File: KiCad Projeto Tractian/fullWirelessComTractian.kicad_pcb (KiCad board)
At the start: 4 copper layers, 46.8 x 53.3 mm, 28 parts, among them U1 ESP8266EX, U2 MX25R3235FM2xx1, U4 MX25R3235FM2xx1, U5 AMS1117-3.3, U6 TMP36xS, Y2 XTAL 16Mhz ±10ppm (TSX -3225 )

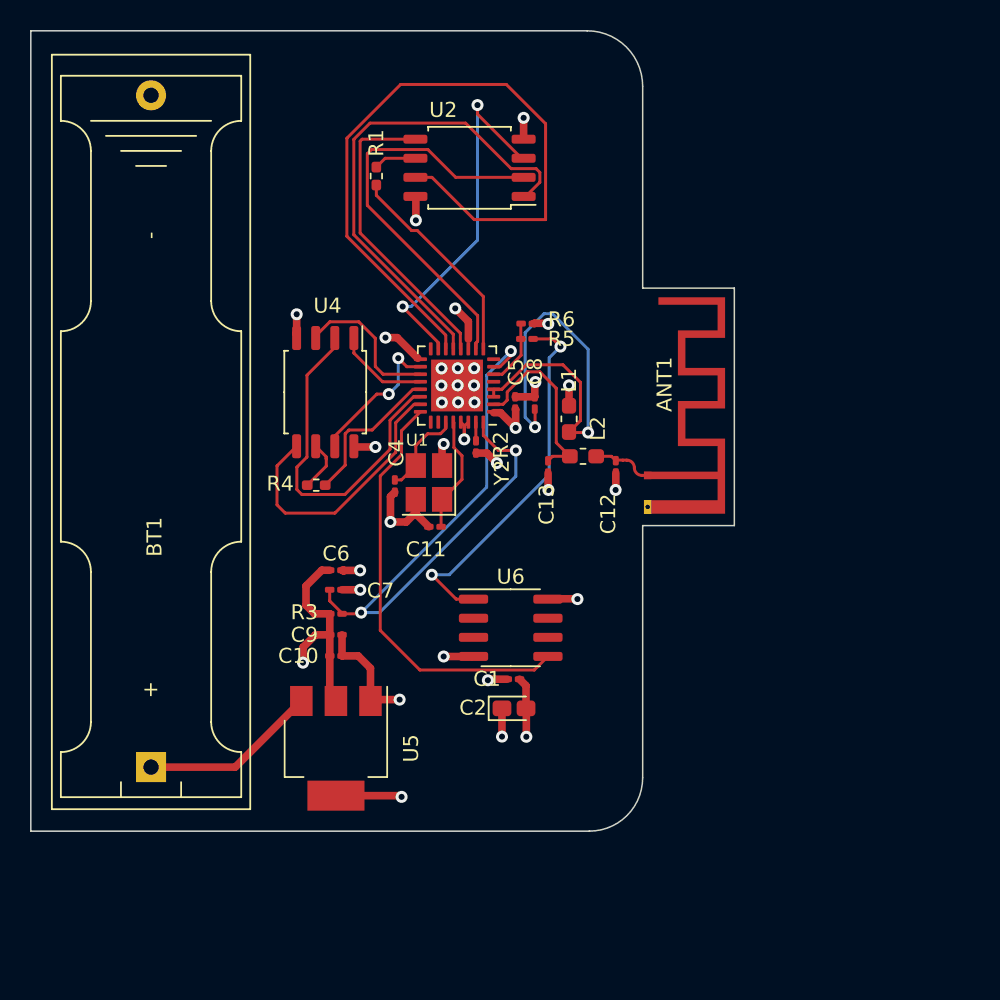
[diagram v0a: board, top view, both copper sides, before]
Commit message: :construction: Add tantos GND vias quanto possível para melhor aterramento -  RF design ESP datasheet
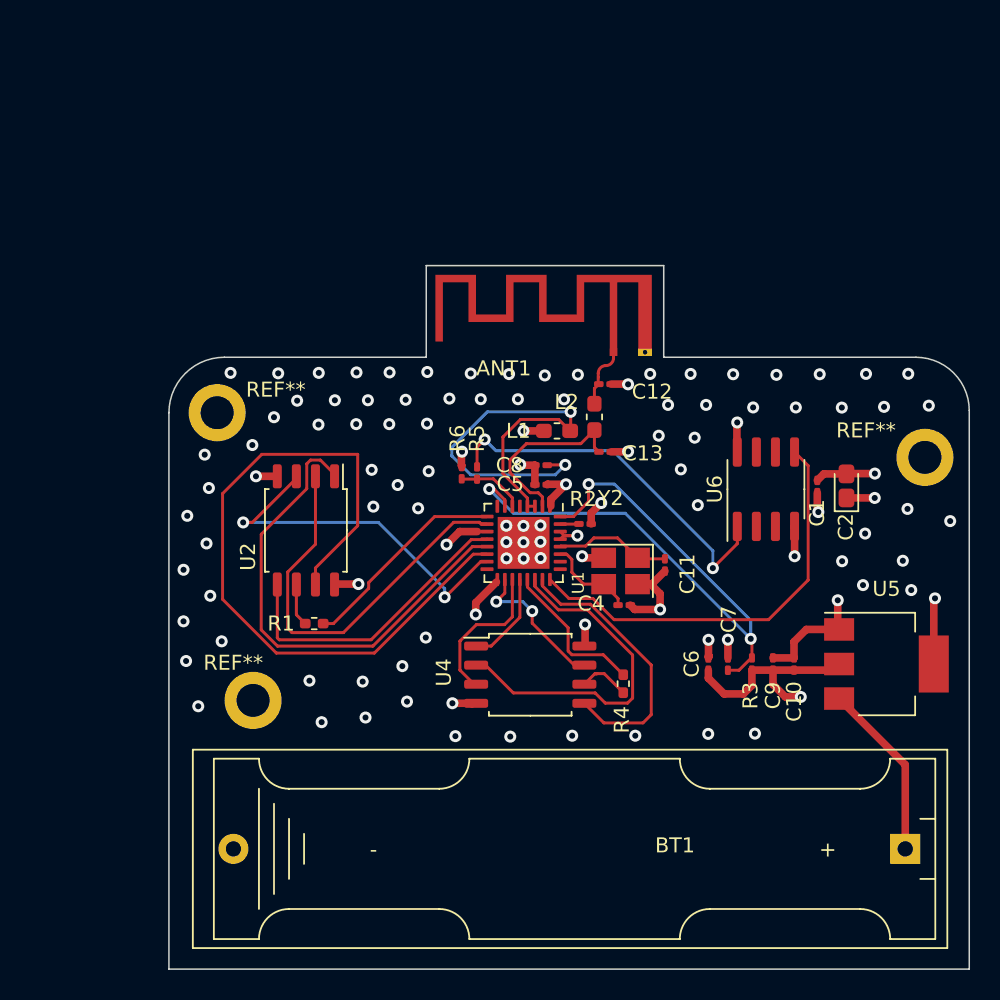
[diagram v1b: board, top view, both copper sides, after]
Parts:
- added REF**: MountingHole_2.2mm_M2_DIN965_Pad, MountingHole:MountingHole_2.2mm_M2_DIN965_Pad, F.Cu at (178.5, 99.2)
- added REF**: MountingHole_2.2mm_M2_DIN965_Pad, MountingHole:MountingHole_2.2mm_M2_DIN965_Pad, F.Cu at (131.4, 96.2)
- added REF**: MountingHole_2.2mm_M2_DIN965_Pad, MountingHole:MountingHole_2.2mm_M2_DIN965_Pad, F.Cu at (133.8, 115.3)
- moved BT1 50.5 mm to (177.2, 125.2), turned to 180 degrees
- moved U5 37.1 mm to (175.9, 112.9), turned to 0 degrees
- moved C10 30.5 mm to (169.8, 112.9), turned to 90 degrees
- moved R1 30.1 mm to (137.9, 110.2), turned to 180 degrees
- moved C9 29.1 mm to (168.4, 112.9), turned to 90 degrees
- moved R3 27.9 mm to (167.0, 112.9), turned to 90 degrees
- moved C2 26.6 mm to (173.3, 101.1), turned to 90 degrees
- moved C7 26.6 mm to (165.4, 112.9), turned to 90 degrees
- moved U2 26.5 mm to (137.3, 104.0), turned to -90 degrees
- moved C6 25.6 mm to (164.1, 112.9), turned to 90 degrees
- moved R4 24.3 mm to (158.4, 114.2), turned to -90 degrees
- moved C1 23.9 mm to (171.3, 101.1), turned to 90 degrees
- moved U4 23.2 mm to (152.2, 113.6), turned to 0 degrees
- moved U6 19.3 mm to (167.9, 101.3), turned to 90 degrees
- moved C4 17.2 mm to (158.5, 109.0), turned to 0 degrees
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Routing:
- net GND: vias 23 -> 100
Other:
- board size 46.8 x 53.3 mm -> 53.3 x 46.8 mm

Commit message: 1 - :rocket: | 2 :memo: | 1 - Final PCB and Gerbers | 2 - Add doc TMP36
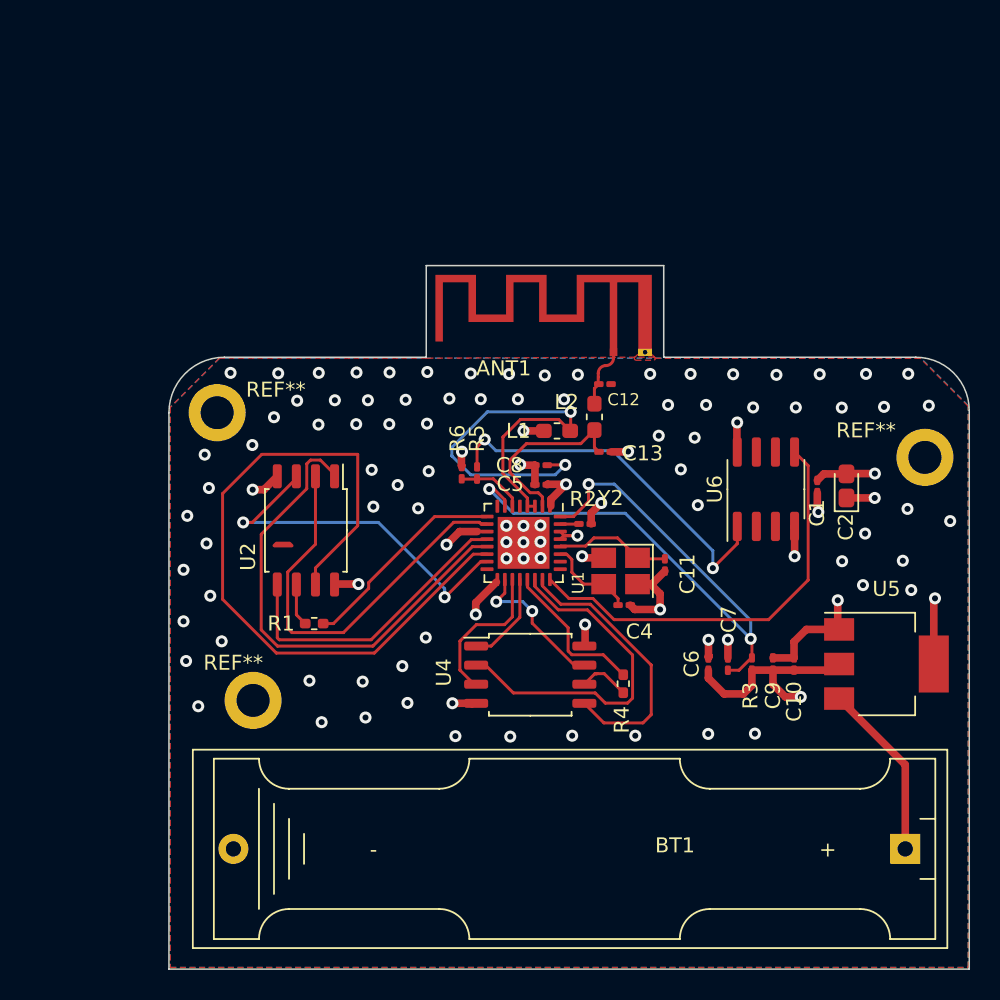
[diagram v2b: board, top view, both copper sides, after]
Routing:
- net GND: track 161.7 -> 404.8 mm, vias 100 -> 99
- added copper zone on B.Cu, net GND
- added copper zone on F.Cu, net GND
- added copper zone on In1.Cu, net GND

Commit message: :bug: fix da Read subroutine
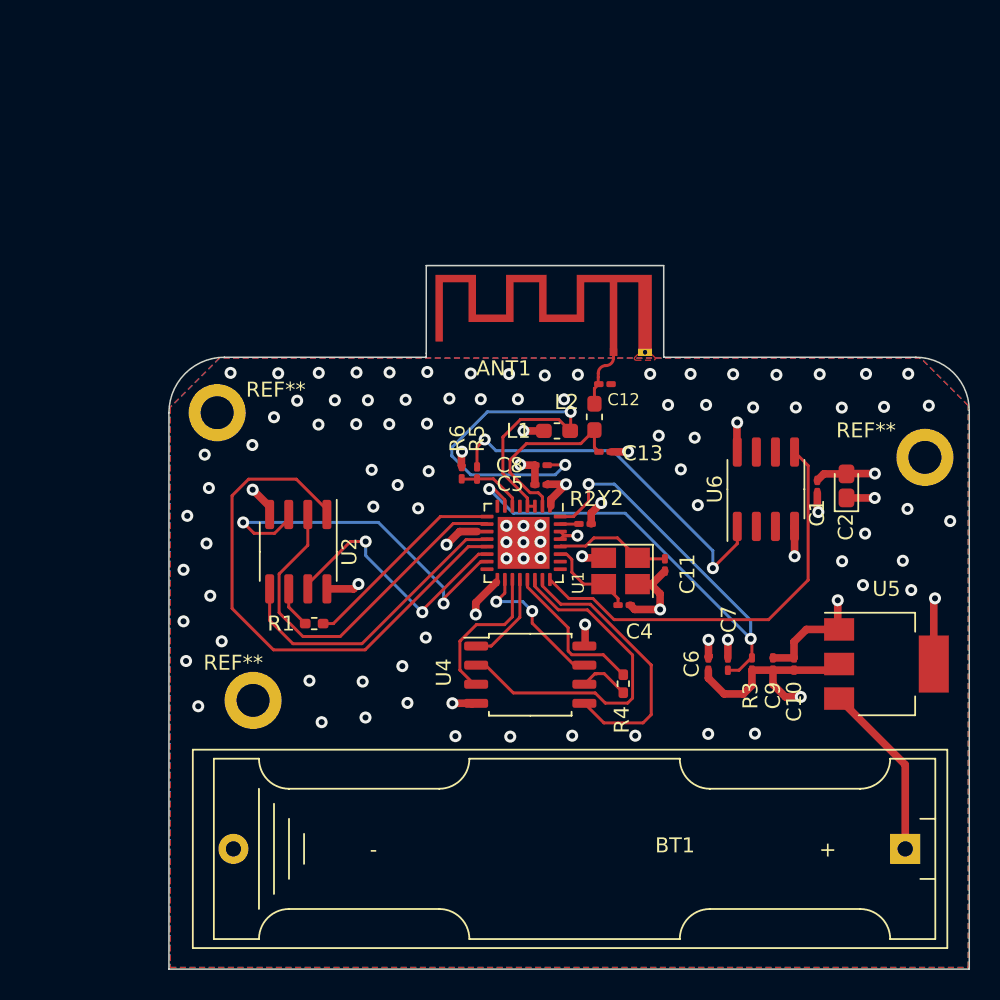
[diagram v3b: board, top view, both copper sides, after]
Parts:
- U2: value MX25R3235FM2xx1 -> AT25SF081-SSHD-X; footprint Package_SO:SOP-8_5.28x5.23mm_P1.27mm -> Package_SO:SOIC-8_3.9x4.9mm_P1.27mm
- moved U2 1.50 mm to (136.8, 105.5)
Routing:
- net DMHD: track 48.7 -> 17.6 mm, vias 0 -> 2
- net DMCS: track 33.0 -> 36.4 mm
- net DMSO: track 27.4 -> 24.9 mm
- net VDD33: track 138.5 -> 139.1 mm
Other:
- outline, holes or cut-outs redrawn

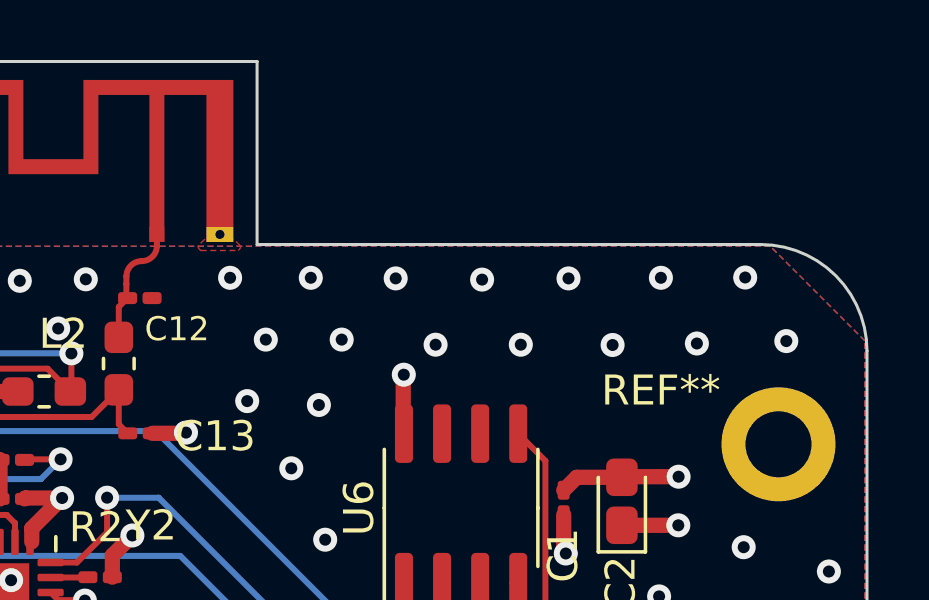
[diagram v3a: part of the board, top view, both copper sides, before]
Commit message: :rocket: Read (right this time) 1024 bytes of data Function
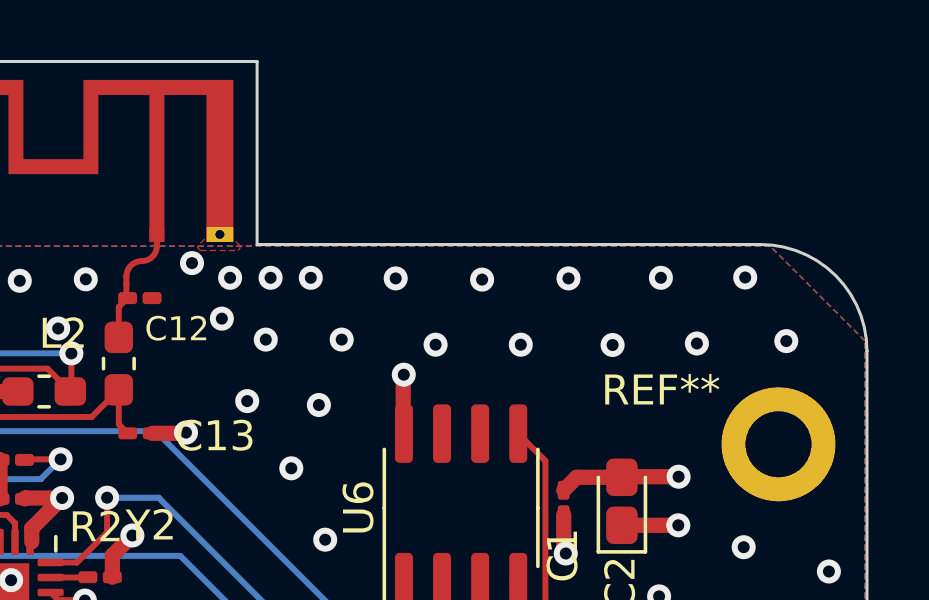
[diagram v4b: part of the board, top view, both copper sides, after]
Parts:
- U6: value TMP36xS -> TMP35
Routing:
- net GND: track 404.9 -> 406.4 mm, vias 99 -> 102
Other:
- outline, holes or cut-outs redrawn
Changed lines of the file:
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@@
         (effects (font (size 1 1) (thickness 0.15)))
     )
-    (fp_text value "TMP36xS" (at 0 3.4 90) (layer "F.Fab") hide
+    (fp_text value "TMP35" (at 0 3.4 90) (layer "F.Fab") hide
         (effects (font (size 1 1) (thickness 0.15)))
     )
@@
   (gr_arc (start 177.89 92.519944) (mid 180.400269 93.559731) (end 181.440056 96.07)
     (stroke (width 0.1) (type default)) (layer "Edge.Cuts"))
-  (gr_line (start 177.89 92.519944) (end 161.11 92.519944)
+  (gr_line (start 177.89 92.519944) (end 161.52 92.519944)
     (stroke (width 0.1) (type default)) (layer "Edge.Cuts"))
   (gr_line (start 128.189784 96.21) (end 128.189784 133.23)
@@
     (stroke (width 0.1) (type default)) (layer "Edge.Cuts"))
   (gr_arc (start 128.189784 96.209377) (mid 129.270623 93.6) (end 131.88 92.519161)
+    (stroke (width 0.1) (type default)) (layer "Edge.Cuts"))
+  (gr_line (start 161.52 92.519944) (end 161.11 92.519944)
     (stroke (width 0.1) (type default)) (layer "Edge.Cuts"))
   (gr_line (start 128.19 133.23) (end 181.44 133.23)
@@
   (via (at 143.41 101.02) (size 0.8) (drill 0.4) (layers "F.Cu" "B.Cu") (free) (net 6))
   (via (at 140.65 96.97) (size 0.8) (drill 0.4) (layers "F.Cu" "B.Cu") (free) (net 6))
+  (via (at 159.934725 94.991652) (size 0.8) (drill 0.4) (layers "F.Cu" "B.Cu") (free) (net 6))
   (via (at 138.35 116.8) (size 0.8) (drill 0.4) (layers "F.Cu" "B.Cu") (free) (net 6))
   (via (at 147.05 115.54) (size 0.8) (drill 0.4) (layers "F.Cu" "B.Cu") (free) (net 6))
@@
   (via (at 139.23 95.38) (size 0.8) (drill 0.4) (layers "F.Cu" "B.Cu") (free) (net 6))
   (via (at 177.58 108.01) (size 0.8) (drill 0.4) (layers "F.Cu" "B.Cu") (free) (net 6))
+  (via (at 161.56 93.63) (size 0.8) (drill 0.4) (layers "F.Cu" "B.Cu") (free) (net 6))
   (via (at 177.02 106.06) (size 0.8) (drill 0.4) (layers "F.Cu" "B.Cu") (free) (net 6))
   (via (at 133.74 98.36) (size 0.8) (drill 0.4) (layers "F.Cu" "B.Cu") (free) (net 6))
@@
   (via (at 135.46 93.59) (size 0.8) (drill 0.4) (layers "F.Cu" "B.Cu") (free) (net 6))
   (via (at 145.28 111.17) (size 0.8) (drill 0.4) (layers "F.Cu" "B.Cu") (free) (net 6))
+  (via (at 158.94 93.14) (size 0.8) (drill 0.4) (layers "F.Cu" "B.Cu") (free) (net 6))
   (via (at 163.93 95.69) (size 0.8) (drill 0.4) (layers "F.Cu" "B.Cu") (free) (net 6))
   (via (at 150.64 104.82) (size 0.8) (drill 0.4) (layers "F.Cu" "B.Cu") (net 6))
@@
   (segment (start 155.5495 105.89) (end 152.99 105.89) (width 0.508) (layer "In1.Cu") (net 6))
   (segment (start 138.16 93.56) (end 140.64 93.56) (width 0.508) (layer "In1.Cu") (net 6))
+  (segment (start 160.21 94.716377) (end 159.934725 94.991652) (width 0.508) (layer "In1.Cu") (net 6))
   (segment (start 172.69 108.63) (end 169.82 105.76) (width 0.508) (layer "In1.Cu") (net 6))
   (segment (start 136.72 95.41) (end 139.2 95.41) (width 0.508) (layer "In1.Cu") (net 6))
@@
   (segment (start 150.65 105.9) (end 147.05 109.5) (width 0.508) (layer "In1.Cu") (net 6))
   (segment (start 174.51 104.56) (end 172.98 106.09) (width 0.508) (layer "In1.Cu") (net 6))
+  (segment (start 160.21 93.63) (end 160.21 94.716377) (width 0.508) (layer "In1.Cu") (net 6))
   (segment (start 136.72 95.58) (end 138.14 97) (width 0.508) (layer "In1.Cu") (net 6))
   (segment (start 135.46 93.59) (end 138.13 93.59) (width 0.508) (layer "In1.Cu") (net 6))
@@
   (segment (start 168.084 109.98) (end 157.81 109.98) (width 0.2) (layer "F.Cu") (net 32))
   (zone (net 6) (net_name "GND") (layer "F.Cu") (name "GND Plane 1 For RF") (hatch edge 0.1)
-    (priority 1)
     (connect_pads (clearance 0.1))
     (min_thickness 0.25) (filled_areas_thickness no)
@@
     (polygon
       (pts
-        (xy 160.48 92.72)
-        (xy 160.55 92.65)
-        (xy 160.55 92.56)
-        (xy 160.33 92.34)
-        (xy 159.37 92.34)
-        (xy 159.15 92.56)
-        (xy 159.15 92.64)
-        (xy 159.23 92.72)
+        (xy 160.47 92.72)
+        (xy 160.54 92.65)
+        (xy 160.54 92.56)
+        (xy 160.32 92.34)
+        (xy 159.36 92.34)
+        (xy 159.14 92.56)
+        (xy 159.14 92.64)
+        (xy 159.22 92.72)
       )
     )

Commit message: :memo: Updates on the documentation | Preliminares, Introduction and Part of Schematics and PCB Design
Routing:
- added copper zone on In2.Cu, net GND
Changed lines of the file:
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@@
+    )
+  )
+  (zone (net 6) (net_name "GND") (layer "In2.Cu") (hatch edge 0.5)
+    (priority 1)
+    (connect_pads (clearance 0.1))
+    (min_thickness 0.25) (filled_areas_thickness no)
+    (fill yes (thermal_gap 0.5) (thermal_bridge_width 0.5))
+    (polygon
+      (pts
+        (xy 181.37 133.12)
+        (xy 181.37 95.74)
+        (xy 178.22 92.59)
+        (xy 131.52 92.59)
+        (xy 128.26 95.85)
+        (xy 128.26 133.12)
+      )
     )
   )
